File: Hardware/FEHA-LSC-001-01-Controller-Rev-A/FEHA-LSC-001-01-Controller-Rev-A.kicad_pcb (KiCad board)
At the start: 2 copper layers, 0 parts

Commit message: LSC layout decisions DEC-30..33: 50 x 25 mm 4-layer, antenna notch, debug header at OUT end
Board updated from schematic (F8, footprints unplaced). scripts/fit_placement.py holds the
agreed placement and its courtyard check. Spec §0 lists the next steps.

Co-Authored-By: Claude Opus 5.5 <noreply@anthropic.com>
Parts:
- added C1: 100nF, PCM_JLCPCB:C_0402, F.Cu at (133.7, 111.4)
- added C10: 1uF, PCM_JLCPCB:C_0805, F.Cu at (134.5, 128.6)
- added C2: 1uF, PCM_JLCPCB:C_0402, F.Cu at (133.7, 113.2)
- added C3: 10uF, PCM_JLCPCB:C_1206, F.Cu at (148.2, 119.2)
- added C4: 10uF, PCM_JLCPCB:C_0603, F.Cu at (138.6, 128.2)
- added C5: 22uF, PCM_JLCPCB:C_1206, F.Cu at (148.2, 122.6)
- added C6: 100nF, PCM_JLCPCB:C_0402, F.Cu at (133.7, 115.1)
- added C7: 100nF, PCM_JLCPCB:C_0402, F.Cu at (133.7, 116.9)
- added C8: 10uF, PCM_JLCPCB:C_1206, F.Cu at (148.2, 125.9)
- added C9: 100nF, PCM_JLCPCB:C_0402, F.Cu at (133.7, 118.8)
- added CN1: HDGC4001SMD-S-2P, _FEHA-LSC-001:CONN-SMD_2P-P4.00_HDGC4001SMD-S-2P, F.Cu at (121.7, 102.3)
- added CN2: HDGC4001SMD-S-2P, _FEHA-LSC-001:CONN-SMD_2P-P4.00_HDGC4001SMD-S-2P, F.Cu at (130.9, 102.3)
- added CN3: USB_DEBUG, _FEHA-LSC-001:PinHeader_1x04_P2.54mm_Vertical_Lock, F.Cu at (143.1, 119.8)
- added D1: SS34, PCM_JLCPCB:D_SMA, F.Cu at (139.5, 97.7)
- added D2: SMBJ26A, PCM_JLCPCB:D_SMB, F.Cu at (136.5, 124.3)
- added D3: Yellow, PCM_JLCPCB:D_0805, F.Cu at (137.7, 108.2)
- added D4: B5819W SL, PCM_JLCPCB:D_SOD-123, F.Cu at (138.4, 101.7)
- added D5: BZT52C10, PCM_JLCPCB:D_SOD-123, F.Cu at (138.4, 105.0)
- added L1: 10uH, _FEHA-LSC-001:IND-SMD_L4.4-W4.2, F.Cu at (144.5, 102.7)
- added Q1: HL2310A, PCM_JLCPCB:Q_SOT-23, F.Cu at (150.1, 102.4)
- added Q2: SI2356DS-T1-GE3, _FEHA-LSC-001:SOT-23_L2.9-W1.3-P1.90-LS2.4-BR, F.Cu at (143.4, 107.6)
- added R1: 10kΩ, PCM_JLCPCB:R_0402, F.Cu at (133.7, 120.6)
- added R10: 100Ω, PCM_JLCPCB:R_0402, F.Cu at (139.4, 115.1)
- added R2: 10kΩ, PCM_JLCPCB:R_0402, F.Cu at (136.5, 111.4)
- added R3: 100kΩ, PCM_JLCPCB:R_0402, F.Cu at (136.5, 113.2)
- added R4: 10kΩ, PCM_JLCPCB:R_0402, F.Cu at (136.5, 115.1)
- added R5: 51kΩ, PCM_JLCPCB:R_0402, F.Cu at (136.5, 116.9)
- added R6: 22kΩ, PCM_JLCPCB:R_0402, F.Cu at (136.5, 118.8)
- added R7: 470Ω, PCM_JLCPCB:R_0402, F.Cu at (136.5, 120.6)
- added R8: 10kΩ, PCM_JLCPCB:R_0402, F.Cu at (139.4, 111.4)
- added R9: 10kΩ, PCM_JLCPCB:R_0402, F.Cu at (139.4, 113.2)
- added S1: Tactile Button, 160gf, PCM_JLCPCB:SW_TS-1088-AR02016, F.Cu at (147.1, 97.7)
- added TP1: GND, TestPoint:TestPoint_Pad_D1.5mm, F.Cu at (142.6, 112.2)
- added TP3: EN, TestPoint:TestPoint_Pad_D1.5mm, F.Cu at (142.6, 115.8)
- added TP4: +24V, TestPoint:TestPoint_Pad_D1.5mm, F.Cu at (146.1, 112.2)
- added TP5: +3V3, TestPoint:TestPoint_Pad_D1.5mm, F.Cu at (146.1, 115.8)
- added TP6: LED_N, TestPoint:TestPoint_Pad_D1.5mm, F.Cu at (149.7, 112.2)
- added TP7: GND, TestPoint:TestPoint_Pad_D1.5mm, F.Cu at (149.7, 115.8)
- added U1: TPS560430XFDBVR, _FEHA-LSC-001:SOT-23-6_L2.9-W1.6-P0.95-LS2.8-BR, F.Cu at (150.1, 106.8)
- added U2: ESP32-C3-MINI-1-H4X(4MB), _FEHA-LSC-001:WIFIM-SMD_ESP32-C3-MINI-1, F.Cu at (124.9, 122.2)

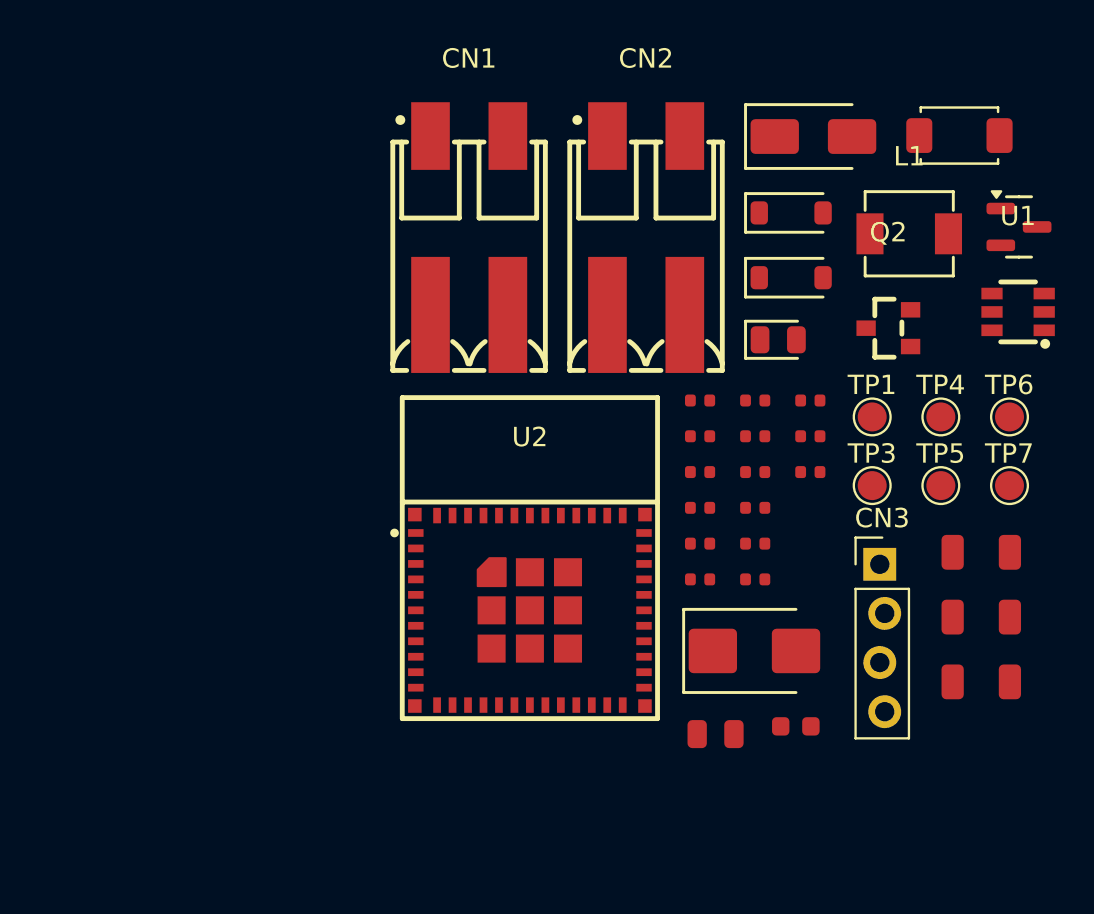
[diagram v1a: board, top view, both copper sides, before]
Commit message: LSC layout steps 1-2: placement applied, board set up (DEC-34)
Placement from fit_placement.py (C5 moved 0.2 mm to clear L1's pad).
setup_board.py: 4 layers, notch outline with 0.5 mm fillets, origin at
the centre, CON-3 and antenna keep-out rule areas, GND pours L1-L4.
Board rules: edge clearance 0.3 mm, via min 0.4 / annular 0.075 (DEC-34);
netclasses per DEC-33 (GND removed from PWR_1A).

Co-Authored-By: Claude Opus 5.5 <noreply@anthropic.com>
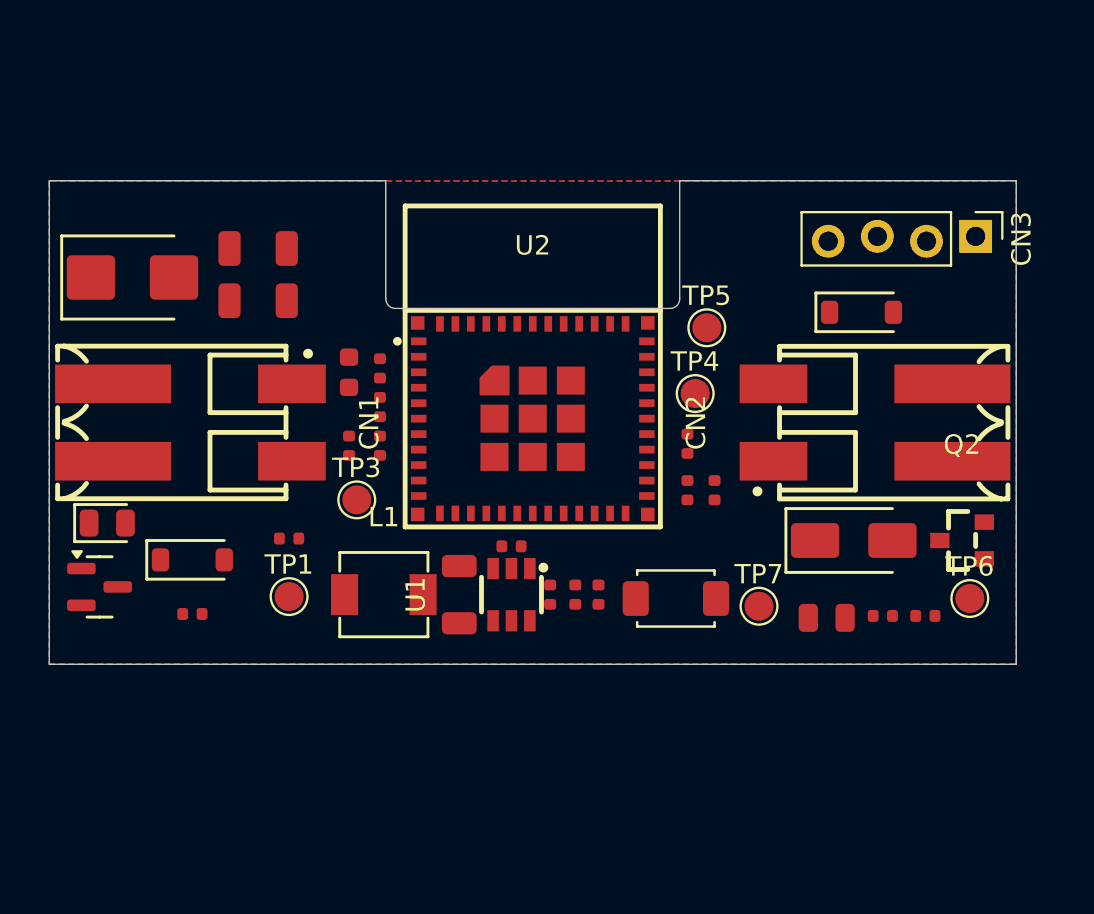
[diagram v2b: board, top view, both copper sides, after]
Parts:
- moved Q1 51.1 mm to (102.6, 121.0)
- moved C8 42.3 mm to (110.8, 106.2)
- moved C3 40.6 mm to (110.8, 103.5)
- moved D2 37.5 mm to (104.3, 105.0)
- moved D3 36.0 mm to (103.0, 117.7)
- moved D5 34.2 mm to (107.4, 119.6)
- moved L1 33.0 mm to (117.3, 121.4)
- moved TP1 31.6 mm to (112.4, 121.5)
- moved R3 30.5 mm to (107.4, 122.4)
- moved U1 30.0 mm to (123.9, 121.4), turned to 90 degrees
- moved C4 29.5 mm to (115.5, 109.9), turned to 90 degrees
- moved S1 28.1 mm to (132.4, 121.6)
- moved C5 27.0 mm to (121.2, 121.4), turned to 90 degrees
- moved TP3 26.7 mm to (115.9, 116.5)
- moved R7 24.2 mm to (112.4, 118.5)
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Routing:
- added copper zone on B.Cu, net GND
- added copper zone on F.Cu, net GND
- added copper zone on In1.Cu, net GND
- added copper zone on In2.Cu, net GND
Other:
- board outline added: 50 x 25 mm
- copper layers 2 -> 4

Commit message: LSC board 50 x 30 mm (DEC-35), buck block placed, SW and VIN pours
Karl's buck placement (14.2 x 9.3 mm block) did not fit under the module
on 50 x 25; board widened to 50 x 30, +Y-referenced parts up 5 mm, CN1/CN2
kept centred. DEC-35 supersedes the DEC-30 board size; CON-2 updated.
F.Cu pours, priority 1, solid connection: /SW hugging U1.6/C7.2/L1.2;
/+24V on U1 VIN pins and C3/C8/C9 pin 1, kept off the IC interior so GND
reaches U1 pin 2. setup_board.py takes the width and keeps hand-drawn pours.

Co-Authored-By: Claude Opus 5.5 <noreply@anthropic.com>
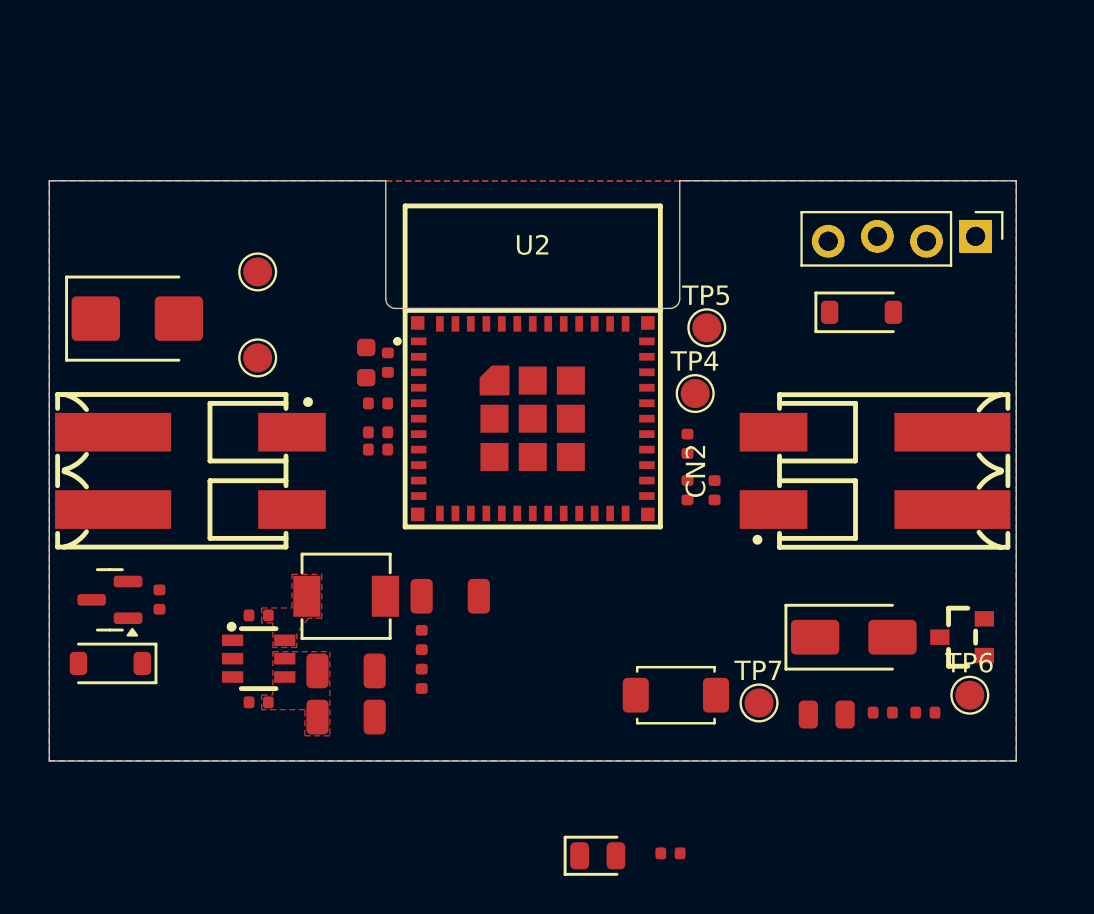
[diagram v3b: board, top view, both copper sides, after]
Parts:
- moved D3 30.6 mm to (128.4, 134.9)
- moved R7 25.6 mm to (132.1, 134.8)
- moved C3 22.3 mm to (115.3, 125.3)
- moved C8 22.0 mm to (115.3, 127.7)
- moved TP1 16.9 mm to (110.8, 104.7)
- moved C9 16.1 mm to (110.8, 127.0), turned to 180 degrees
- moved C7 13.6 mm to (110.8, 122.5)
- moved U1 13.5 mm to (110.8, 124.7), turned to 180 degrees
- moved R6 10.1 mm to (119.3, 125.8), turned to -90 degrees
- moved TP3 8.95 mm to (110.8, 109.2)
- moved R5 8.28 mm to (119.3, 123.7), turned to -90 degrees
- moved D5 6.83 mm to (103.2, 125.0), turned to 180 degrees
- moved C10 5.00 mm to (140.2, 127.6)
- moved D1 5.00 mm to (141.6, 123.6)
- moved Q2 5.00 mm to (147.2, 123.6)
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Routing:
- added copper zone on F.Cu, net /+24V
- added copper zone on F.Cu, net /SW
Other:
- board size 50 x 25 mm -> 50 x 30 mm

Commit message: LSC netclass PWR_3V3 and pre-defined sizes (DEC-36); Karl's layout edits
PWR_3V3 0.6 mm on +3V3 (buck output to the module's radio peaks).
Pre-defined track widths 0.25/0.4/0.6/1.0 mm and via 0.45/0.3.
DEC-33 netclass part superseded by DEC-36. Board: Karl's placement and
layout edits since c345fb3 (saved with zones unfilled; refill with B).

Co-Authored-By: Claude Opus 5.5 <noreply@anthropic.com>
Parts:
- moved TP4 24.1 mm to (110.8, 102.6)
- moved TP5 20.8 mm to (121.3, 124.1)
- moved R10 19.7 mm to (127.4, 119.2), turned to -90 degrees
- moved TP6 18.5 mm to (146.7, 108.1)
- moved R7 17.9 mm to (123.4, 119.2), turned to -90 degrees
- moved TP7 15.4 mm to (121.3, 127.4)
- moved D4 13.9 mm to (144.6, 120.5), turned to 180 degrees
- moved D1 11.7 mm to (133.7, 115.0), turned to 90 degrees
- moved C10 8.94 mm to (134.7, 120.6)
- moved D3 8.51 mm to (129.2, 126.4), turned to 180 degrees
- moved R9 7.45 mm to (137.7, 122.4), turned to -90 degrees
- moved R2 7.30 mm to (128.3, 119.2)
- moved CN3 7.17 mm to (142.9, 108.1)
- moved Q2 6.94 mm to (140.4, 122.4), turned to 180 degrees
- moved S1 5.41 mm to (129.2, 122.2)
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
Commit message: LSC narrower track widths (DEC-37): PWR_3V3 0.5 mm, sizes 0.25/0.3/0.5/1.0
Pre-defined sizes 0.4 -> 0.3 and 0.6 -> 0.5; PWR_3V3 netclass 0.6 -> 0.5.
The two +3V3 segments already routed at 0.6 set to 0.5. DRC unchanged.
Spec section 0 notes carried along.

Co-Authored-By: Claude Opus 5.5 <noreply@anthropic.com>
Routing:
- net +3V3: track 0.00 -> 1.59 mm
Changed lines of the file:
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@@
 		(layer "Edge.Cuts")
+	)
+	(segment
+		(start 119.1 109.9)
+		(end 117.5082 109.9)
+		(width 0.5)
+		(layer "F.Cu")
+		(net "+3V3")
+	)
+	(segment
+		(start 117.5082 109.9)
+		(end 117.507 109.9012)
+		(width 0.5)
+		(layer "F.Cu")
+		(net "+3V3")
 	)
 	(zone

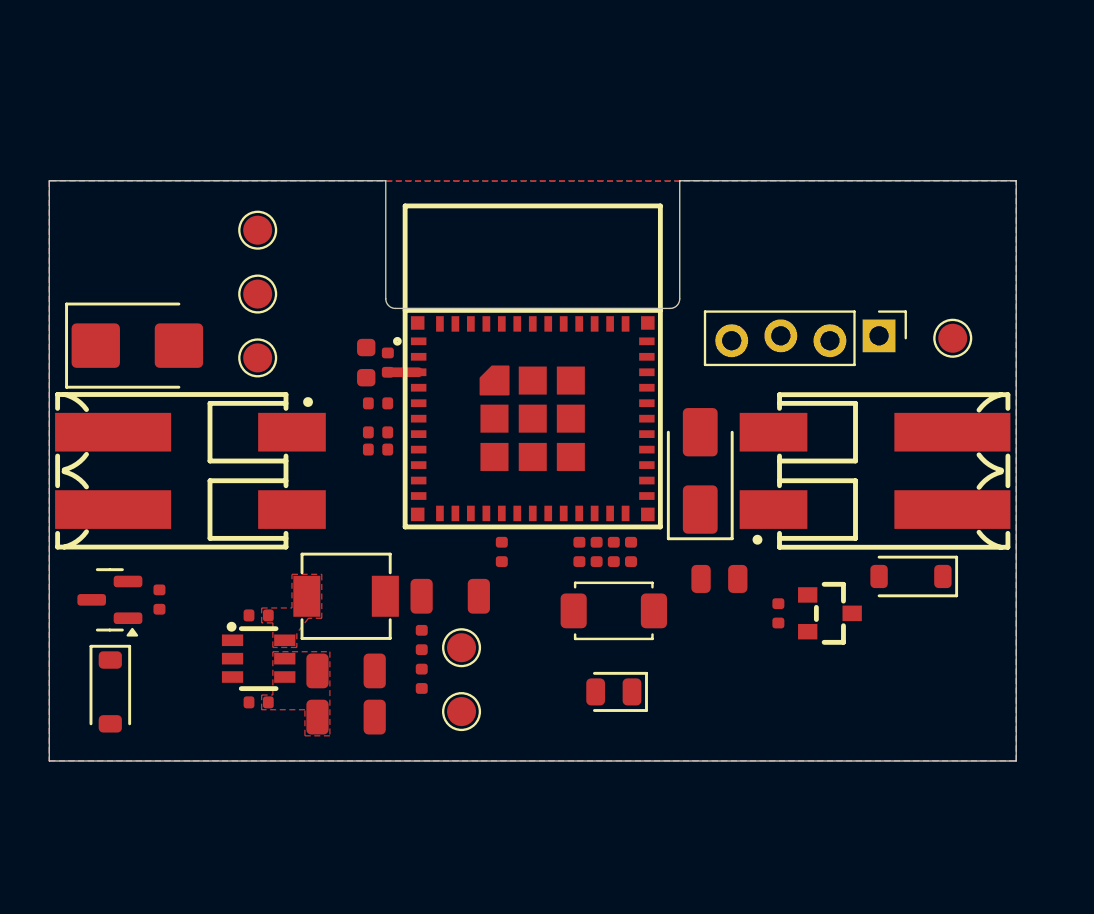
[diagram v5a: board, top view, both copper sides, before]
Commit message: LSC routing complete; polarity silkscreen at CN1/CN2
Karl's routing (DRC 0 unconnected). F.SilkS +/- enlarged to 1.4 mm at
both connectors plus IN/OUT; B.SilkS +/- and IN/OUT at 2.5 mm behind the
pins. .kicad_pro change is KiCad's netclass reordering on save.

Co-Authored-By: Claude Opus 5.5 <noreply@anthropic.com>
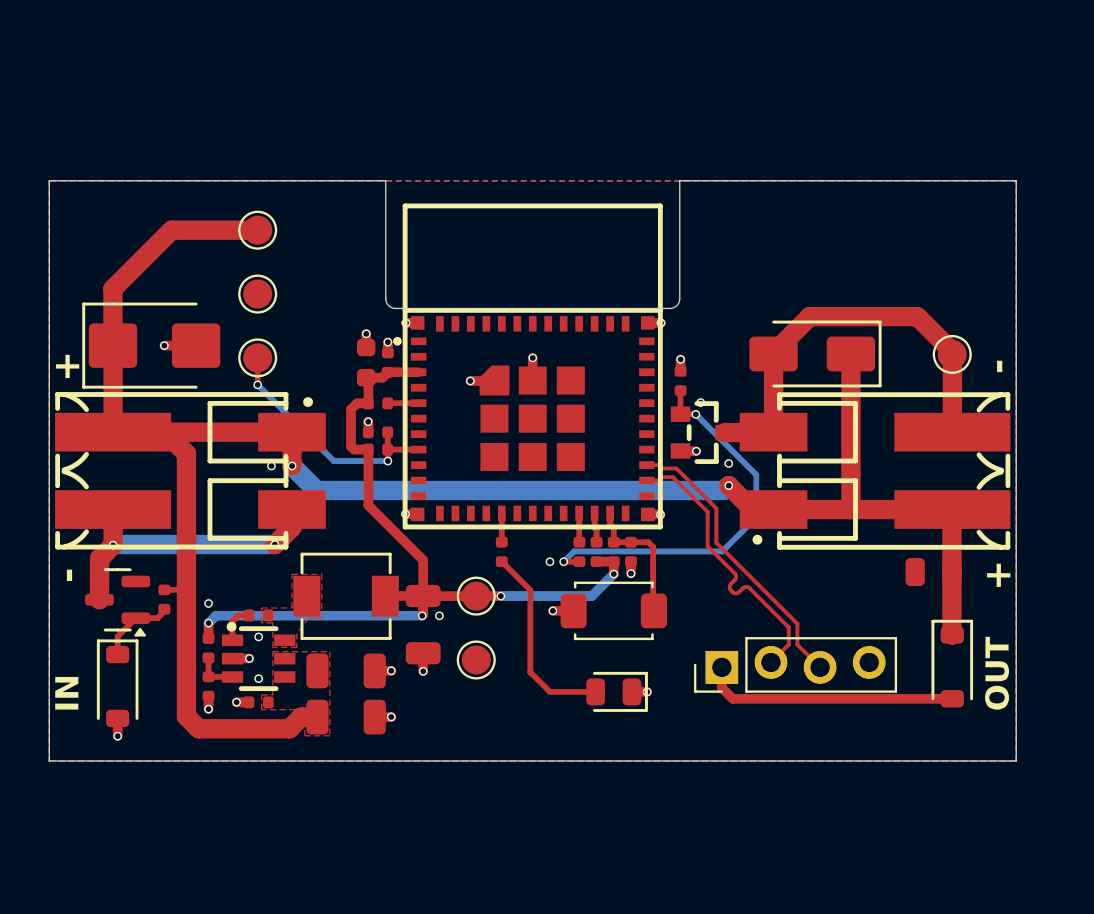
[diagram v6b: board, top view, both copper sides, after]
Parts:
- moved CN3 18.7 mm to (134.8, 125.0), turned to 90 degrees
- moved R9 13.0 mm to (132.6, 110.4), turned to 90 degrees
- moved Q2 11.4 mm to (133.8, 113.0)
- moved C10 11.1 mm to (145.7, 120.2), turned to 180 degrees
- moved R5 11.0 mm to (108.2, 124.2)
- moved R6 11.0 mm to (108.2, 126.2)
- moved D1 8.37 mm to (139.5, 109.0), turned to 180 degrees
- moved D4 5.14 mm to (146.7, 125.1), turned to -90 degrees
- moved TP5 2.77 mm to (122.1, 121.5)
- moved TP7 2.77 mm to (122.1, 124.8)
- moved C5 2.03 mm to (119.3, 123.0), turned to -90 degrees
- moved D2 0.89 mm to (105.4, 108.5)
- moved TP6 0.84 mm to (146.7, 109.0)
- moved D5 0.47 mm to (103.5, 126.2)
- moved Q1 0.41 mm to (103.5, 121.7)
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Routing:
- net /+24V: track 0.00 -> 102.2 mm, vias 0 -> 2
- net +3V3: track 1.59 -> 43.5 mm, vias 0 -> 4
- net /LED_N: track 0.00 -> 21.5 mm
- net /G_OUT: track 0.00 -> 20.3 mm, vias 0 -> 2
- net GND: track 0.00 -> 18.0 mm, vias 0 -> 30
- net /VIN_N: track 0.00 -> 15.5 mm, vias 0 -> 2
- net /USB_MCUD+: track 0.00 -> 15.0 mm
- net /USB_MCUD-: track 0.00 -> 14.9 mm
- net /VBUS: track 0.00 -> 13.2 mm
- net /EN: track 0.00 -> 12.8 mm, vias 0 -> 2
- net Net-(D3-Pad2): track 0.00 -> 10.1 mm
- net /BTN: track 0.00 -> 6.96 mm
- net /G_REV: track 0.00 -> 3.89 mm
- net /FB: track 0.00 -> 2.21 mm
- net Net-(U1-CB): track 0.00 -> 1.96 mm
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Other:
- board text added: "+"
- board text added: "-"
- board text added: "IN"
- board text added: "OUT"

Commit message: LSC logo and name block on B.SilkS; 24 V via pairs, MOSFET source vias, drain pour (DEC-39)
- FEHA logo (copied from GeyserSense into _FEHA-LSC-001) and the
  title / designer / PN block on the back, GeyserSense arrangement.
- Second via at both +24V layer changes; Q1 source 2 GND vias,
  Q2 source second GND via; LED_N drain pour on F.Cu and B.Cu with
  6 stitching vias (Karl adjusted vias, USB pair and EN routing).
- Karl's knockout silkscreen edits. DRC: no new violations,
  0 unconnected.

Co-Authored-By: Claude Opus 5.5 <noreply@anthropic.com>
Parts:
- added G***: Fuchs Elektro & Home Automation, _FEHA-LSC-001:logo, B.Cu at (125.0, 112.3)
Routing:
- net /+24V: track 102.2 -> 106.5 mm, vias 2 -> 4
- net GND: track 18.0 -> 20.8 mm, vias 30 -> 104
- net /LED_N: vias 0 -> 6
- added copper zone on B.Cu, net /LED_N
- added copper zone on F.Cu, net /LED_N
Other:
- board text added: "${TITLE} Designed by ${COMMENT1} PN: ${COMMENT2}"
- board text added: "3V3"
- board text added: "BTN"
- board text added: "D+"
- board text added: "D-"
- board text added: "EN"
- board text added: "G"
- board text added: "GND"
- board text added: "LED"
- board text added: "LED_N"
- board text added: "V"

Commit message: LSC layout gate review; VIN_N via pairs, courtyards, DRC exclusions (DEC-40)
Layout gate review register (checklist v1.3) for FEHA-LSC-001-01 Rev A.
- VIN_N: second 0.45/0.3 via at both layer changes (L-1)
- Courtyards added to Q2, U1, CN1, CN2, L1 footprints (library + board),
  logo exempt, missing_courtyard check back to error (L-3)
- 4 courtyard-margin overlaps and 3 U2 silk/notch warnings excluded in DRC
  (L-7, A-L1); teardrops; TP4 label 24V
- Spec: section 7 rules 3/4/9 and section 10 as built, DEC-40, section 0;
  profile deferrals module-epad-no-vias, courtyard-margin-overlaps

DRC: 0 unconnected, 0 parity, 0 unexcluded errors.

Co-Authored-By: Claude Opus 5.5 <noreply@anthropic.com>
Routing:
- net /VIN_N: track 15.5 -> 16.9 mm, vias 2 -> 4
- net GND: track 20.8 -> 21.6 mm, vias 104 -> 105
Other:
- board text added: "24V"
